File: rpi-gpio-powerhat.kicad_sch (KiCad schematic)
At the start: 1 part, among them J1 rpi-gpio-powerhat

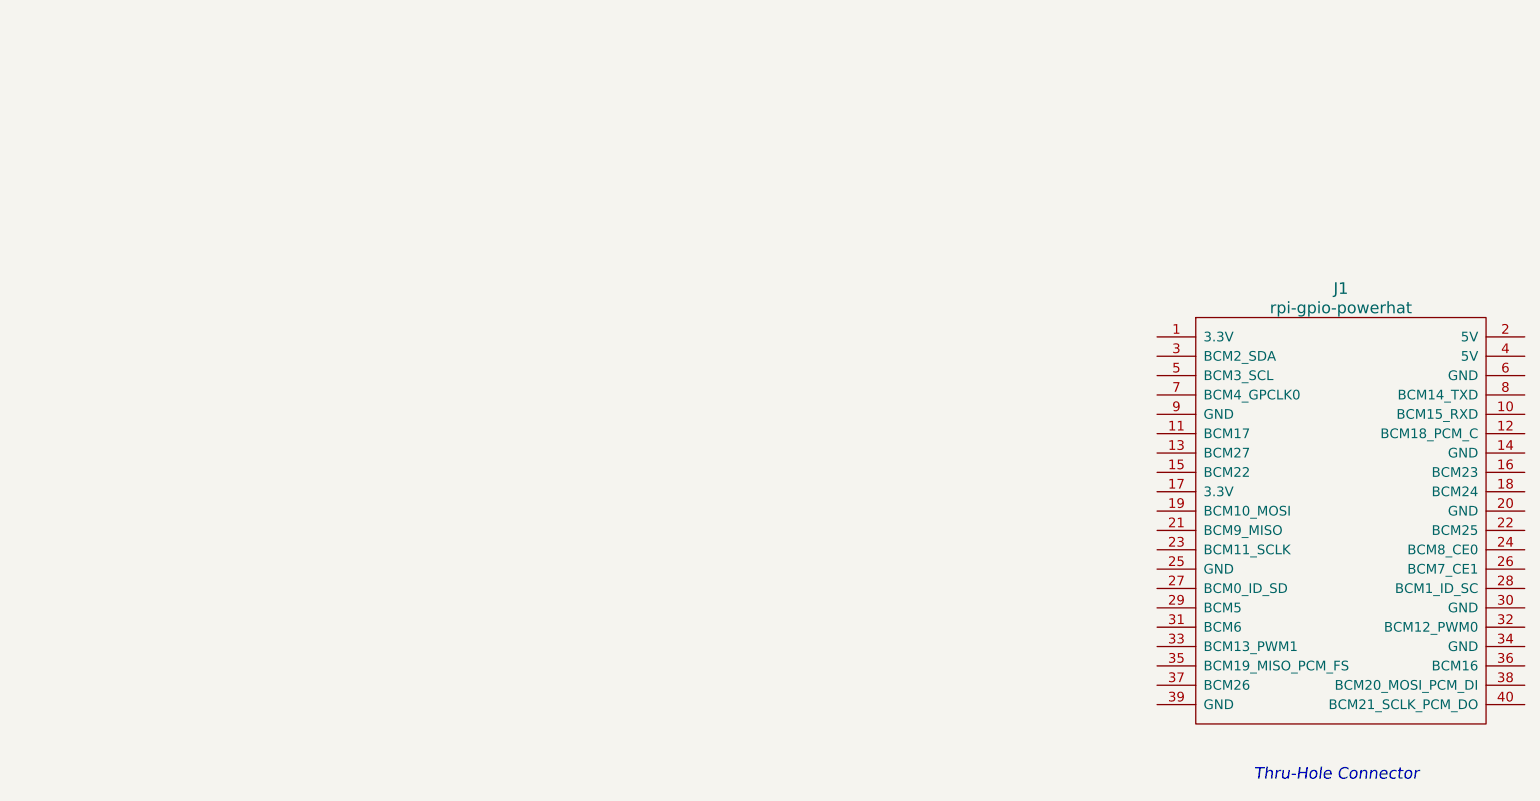
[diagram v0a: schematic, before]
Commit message: Made the powerhat even smaller
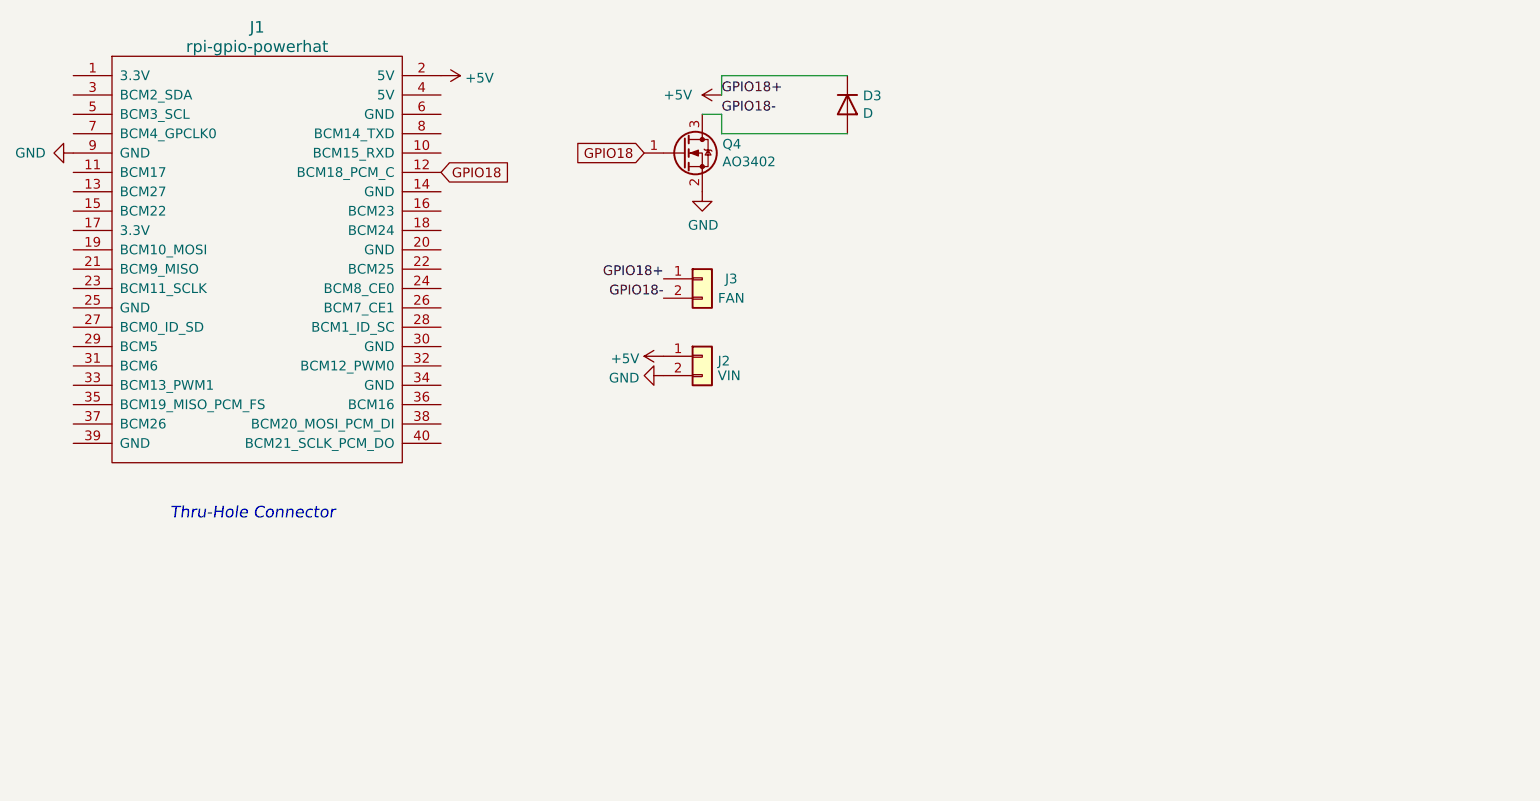
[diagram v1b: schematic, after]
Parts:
- added D3: D, Diode_SMD:D_SOD-123F, symbol Device:D
- added J2: VIN, rpi-powerhat:1546551-2, symbol Connector_Generic:Conn_01x02
- added J3: FAN, Connector_JST:JST_PH_B2B-PH-K_1x02_P2.00mm_Vertical, symbol Connector_Generic:Conn_01x02
- added Q4: AO3402, Package_TO_SOT_SMD:SOT-23, symbol Transistor_FET:DMG3402L
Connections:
- net GPIO18: now reaches J1.12 (BCM18_PCM_C)
- net GPIO18: now also Q4.1 (G)
- net +5V: now reaches J1.2 (5V)
- net +5V: now also D3.1 (K), J2.1 (Pin_1), J3.1 (Pin_1)
- net GND: now reaches J1.9 (GND)
- net GND: now also J2.2 (Pin_2), Q4.2 (S)
- new net GPIO18-: D3.2 (A), J3.2 (Pin_2), Q4.3 (D)
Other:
- moved on the sheet: J1

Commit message: Added recent changes and production files
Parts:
- J1: footprint rpi-powerhat:Pin_Header_Straight_2x20 -> Connector_PinHeader_2.54mm:PinHeader_2x06_P2.54mm_Vertical
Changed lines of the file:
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@@
       (effects (font (size 1.524 1.524)))
     )
-    (property "Footprint" "rpi-powerhat:Pin_Header_Straight_2x20" (at 48.26 34.29 0)
+    (property "Footprint" "Connector_PinHeader_2.54mm:PinHeader_2x06_P2.54mm_Vertical" (at 48.26 34.29 0)
       (effects (font (size 1.524 1.524)) hide)
     )
